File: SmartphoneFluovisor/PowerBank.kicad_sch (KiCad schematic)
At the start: 53 parts, among them J1 USB_A, J2 Conn_01x02_Pin, J3 Conn_01x02, J4 Conn_01x02_Pin, J5 Conn_01x02_Pin, J6 Conn_01x02, J7 Conn_01x02, J8 Conn_01x02_Pin, J9 Conn_01x02_Pin, SW1 SW_Push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

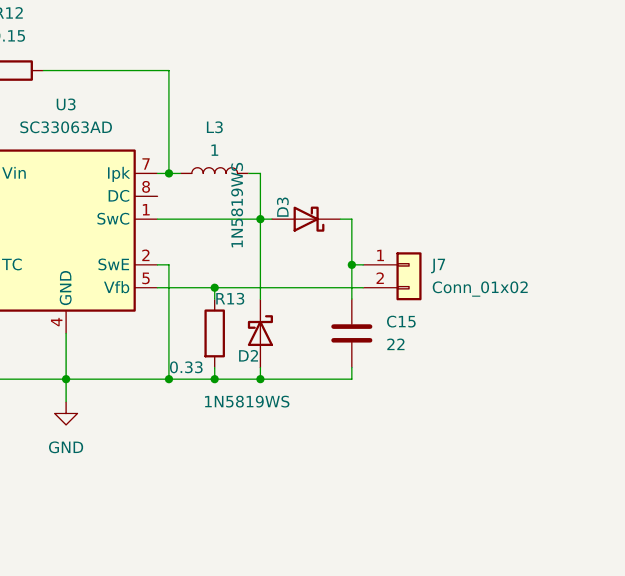
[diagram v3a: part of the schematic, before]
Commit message: v0.7 boost & buck driver are added into the PCB. Seems 2B ready!
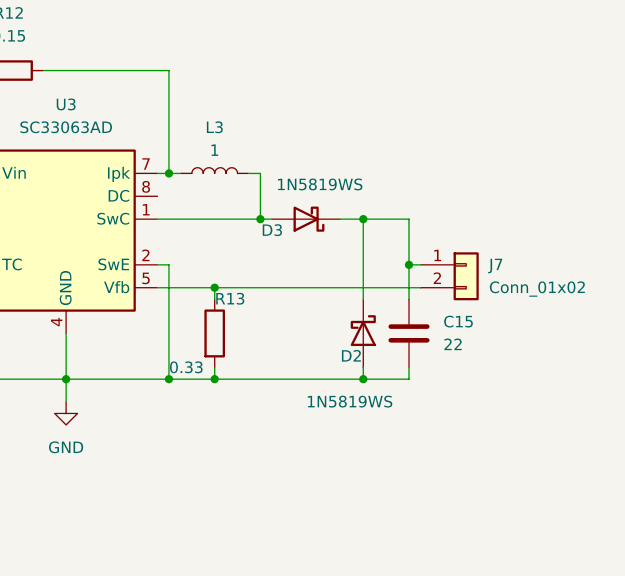
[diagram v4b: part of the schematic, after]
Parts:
- R12: footprint Resistor_SMD:R_0603_1608Metric_Pad0.98x0.95mm_HandSolder -> Resistor_SMD:R_1206_3216Metric_Pad1.30x1.75mm_HandSolder
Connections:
- net at D3.2 (A), L3.2, U3.1 (SwC): no longer D2.1 (K)
- net at C15.1, D3.1 (K), J7.1 (Pin_1): now also D2.1 (K)
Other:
- moved on the sheet: C15, D2, J7
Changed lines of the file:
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@@
   (junction (at 135.89 92.71) (diameter 0) (color 0 0 0 0)
   )
-  (junction (at 256.54 44.45) (diameter 0) (color 0 0 0 0)
+  (junction (at 262.89 44.45) (diameter 0) (color 0 0 0 0)
   )
   (junction (at 143.51 107.95) (diameter 0) (color 0 0 0 0)
@@
   (junction (at 157.48 88.9) (diameter 0) (color 0 0 0 0)
   )
+  (junction (at 257.81 39.37) (diameter 0) (color 0 0 0 0)
+  )
   (junction (at 262.89 142.24) (diameter 0) (color 0 0 0 0)
   )
@@
   (junction (at 158.75 123.19) (diameter 0) (color 0 0 0 0)
   )
-  (junction (at 246.38 57.15) (diameter 0) (color 0 0 0 0)
-  )
   (junction (at 146.05 91.44) (diameter 0) (color 0 0 0 0)
   )
@@
   (junction (at 162.56 80.01) (diameter 0) (color 0 0 0 0)
   )
+  (junction (at 257.81 57.15) (diameter 0) (color 0 0 0 0)
+  )
   (junction (at 182.88 100.33) (diameter 0) (color 0 0 0 0)
   )
@@
     (stroke (width 0) (type default))
   )
-  (wire (pts (xy 256.54 44.45) (xy 256.54 48.26))
+  (wire (pts (xy 262.89 44.45) (xy 262.89 48.26))
     (stroke (width 0) (type default))
   )
@@
     (stroke (width 0) (type default))
   )
-  (wire (pts (xy 256.54 44.45) (xy 257.81 44.45))
+  (wire (pts (xy 262.89 44.45) (xy 264.16 44.45))
     (stroke (width 0) (type default))
   )
@@
     (stroke (width 0) (type default))
   )
-  (wire (pts (xy 256.54 55.88) (xy 256.54 57.15))
+  (wire (pts (xy 262.89 55.88) (xy 262.89 57.15))
     (stroke (width 0) (type default))
   )
@@
     (stroke (width 0) (type default))
   )
-  (wire (pts (xy 246.38 39.37) (xy 246.38 48.26))
-    (stroke (width 0) (type default))
-  )
   (wire (pts (xy 222.25 144.78) (xy 218.44 144.78))
     (stroke (width 0) (type default))
@@
     (stroke (width 0) (type default))
   )
-  (wire (pts (xy 246.38 55.88) (xy 246.38 57.15))
+  (wire (pts (xy 257.81 55.88) (xy 257.81 57.15))
     (stroke (width 0) (type default))
   )
@@
     (stroke (width 0) (type default))
   )
-  (wire (pts (xy 246.38 57.15) (xy 256.54 57.15))
-    (stroke (width 0) (type default))
-  )
   (wire (pts (xy 219.71 120.65) (xy 219.71 132.08))
     (stroke (width 0) (type default))
@@
     (stroke (width 0) (type default))
   )
-  (wire (pts (xy 255.27 39.37) (xy 256.54 39.37))
+  (wire (pts (xy 255.27 39.37) (xy 257.81 39.37))
     (stroke (width 0) (type default))
   )
@@
     (stroke (width 0) (type default))
   )
+  (wire (pts (xy 257.81 39.37) (xy 262.89 39.37))
+    (stroke (width 0) (type default))
+  )
   (wire (pts (xy 143.51 107.95) (xy 152.4 107.95))
     (stroke (width 0) (type default))
@@
     (stroke (width 0) (type default))
   )
+  (wire (pts (xy 257.81 39.37) (xy 257.81 48.26))
+    (stroke (width 0) (type default))
+  )
   (wire (pts (xy 83.82 99.06) (xy 93.98 99.06))
     (stroke (width 0) (type default))
@@
     (stroke (width 0) (type default))
   )
+  (wire (pts (xy 257.81 57.15) (xy 262.89 57.15))
+    (stroke (width 0) (type default))
+  )
   (wire (pts (xy 101.6 85.09) (xy 101.6 87.63))
     (stroke (width 0) (type default))
@@
     (stroke (width 0) (type default))
   )
-  (wire (pts (xy 241.3 57.15) (xy 246.38 57.15))
+  (wire (pts (xy 241.3 57.15) (xy 257.81 57.15))
     (stroke (width 0) (type default))
   )
@@
     (stroke (width 0) (type default))
   )
-  (wire (pts (xy 256.54 39.37) (xy 256.54 44.45))
+  (wire (pts (xy 262.89 39.37) (xy 262.89 44.45))
     (stroke (width 0) (type default))
   )
@@
     (stroke (width 0) (type default))
   )
+  (wire (pts (xy 241.3 46.99) (xy 264.16 46.99))
+    (stroke (width 0) (type default))
+  )
   (wire (pts (xy 207.01 31.75) (xy 207.01 34.29))
     (stroke (width 0) (type default))
@@
     (stroke (width 0) (type default))
   )
-  (wire (pts (xy 241.3 46.99) (xy 257.81 46.99))
-    (stroke (width 0) (type default))
-  )
   (wire (pts (xy 182.88 88.9) (xy 182.88 90.17))
     (stroke (width 0) (type default))
@@
       (effects (font (size 1.27 1.27)))
     )
-    (property "Footprint" "Resistor_SMD:R_0603_1608Metric_Pad0.98x0.95mm_HandSolder" (at 218.44 21.082 90)
+    (property "Footprint" "Resistor_SMD:R_1206_3216Metric_Pad1.30x1.75mm_HandSolder" (at 218.44 21.082 90)
       (effects (font (size 1.27 1.27)) hide)
     )
@@
     )
   )
-  (symbol (lib_id "Diode:1N5819WS") (at 246.38 52.07 270) (unit 1)
+  (symbol (lib_id "Diode:1N5819WS") (at 257.81 52.07 270) (unit 1)
     (in_bom yes) (on_board yes) (dnp no)
-    (property "Reference" "D2" (at 243.84 54.61 90)
-      (effects (font (size 1.27 1.27)) (justify left))
-    )
-    (property "Value" "1N5819WS" (at 240.03 59.69 90)
-      (effects (font (size 1.27 1.27)) (justify left))
-    )
-    (property "Footprint" "Diode_SMD:D_SOD-323_HandSoldering" (at 241.935 52.07 0)
-      (effects (font (size 1.27 1.27)) hide)
-    )
-    (property "Datasheet" "https://datasheet.lcsc.com/lcsc/2204281430_Guangdong-Hottech-1N5819WS_C191023.pdf" (at 246.38 52.07 0)
+    (property "Reference" "D2" (at 255.27 54.61 90)
+      (effects (font (size 1.27 1.27)) (justify left))
+    )
+    (property "Value" "1N5819WS" (at 251.46 59.69 90)
+      (effects (font (size 1.27 1.27)) (justify left))
+    )
+    (property "Footprint" "Diode_SMD:D_SOD-323_HandSoldering" (at 253.365 52.07 0)
+      (effects (font (size 1.27 1.27)) hide)
+    )
+    (property "Datasheet" "https://datasheet.lcsc.com/lcsc/2204281430_Guangdong-Hottech-1N5819WS_C191023.pdf" (at 257.81 52.07 0)
       (effects (font (size 1.27 1.27)) hide)
     )
@@
     )
   )
-  (symbol (lib_id "Connector_Generic:Conn_01x02") (at 262.89 44.45 0) (unit 1)
-    (in_bom yes) (on_board yes) (dnp no) (fields_autoplaced)
-    (property "Reference" "J7" (at 265.43 44.45 0)
-      (effects (font (size 1.27 1.27)) (justify left))
-    )
-    (property "Value" "Conn_01x02" (at 265.43 46.99 0)
-      (effects (font (size 1.27 1.27)) (justify left))
-    )
-    (property "Footprint" "Connector_PinHeader_2.54mm:PinHeader_1x02_P2.54mm_Vertical" (at 262.89 44.45 0)
-      (effects (font (size 1.27 1.27)) hide)
-    )
-    (property "Datasheet" "~" (at 262.89 44.45 0)
+  (symbol (lib_id "Connector_Generic:Conn_01x02") (at 269.24 44.45 0) (unit 1)
+    (in_bom yes) (on_board yes) (dnp no) (fields_autoplaced)
+    (property "Reference" "J7" (at 271.78 44.45 0)
+      (effects (font (size 1.27 1.27)) (justify left))
+    )
+    (property "Value" "Conn_01x02" (at 271.78 46.99 0)
+      (effects (font (size 1.27 1.27)) (justify left))
+    )
+    (property "Footprint" "Connector_PinHeader_2.54mm:PinHeader_1x02_P2.54mm_Vertical" (at 269.24 44.45 0)
+      (effects (font (size 1.27 1.27)) hide)
+    )
+    (property "Datasheet" "~" (at 269.24 44.45 0)
       (effects (font (size 1.27 1.27)) hide)
     )
@@
   (symbol (lib_id "Diode:1N5819WS") (at 251.46 39.37 180) (unit 1)
     (in_bom yes) (on_board yes) (dnp no)
-    (property "Reference" "D3" (at 248.92 36.83 90)
-      (effects (font (size 1.27 1.27)) (justify left))
-    )
-    (property "Value" "1N5819WS" (at 243.84 33.02 90)
+    (property "Reference" "D3" (at 248.92 40.64 0)
+      (effects (font (size 1.27 1.27)) (justify left))
+    )
+    (property "Value" "1N5819WS" (at 257.81 35.56 0)
       (effects (font (size 1.27 1.27)) (justify left))
     )
@@
     )
   )
-  (symbol (lib_id "Device:C") (at 256.54 52.07 0) (unit 1)
-    (in_bom yes) (on_board yes) (dnp no) (fields_autoplaced)
-    (property "Reference" "C15" (at 260.35 50.8 0)
-      (effects (font (size 1.27 1.27)) (justify left))
-    )
-    (property "Value" "22" (at 260.35 53.34 0)
-      (effects (font (size 1.27 1.27)) (justify left))
-    )
-    (property "Footprint" "Capacitor_SMD:C_1206_3216Metric_Pad1.33x1.80mm_HandSolder" (at 257.5052 55.88 0)
-      (effects (font (size 1.27 1.27)) hide)
-    )
-    (property "Datasheet" "~" (at 256.54 52.07 0)
-      (effects (font (size 1.27 1.27)) hide)
-    )
+  (symbol (lib_id "Device:C") (at 262.89 52.07 0) (unit 1)
+    (in_bom yes) (on_board yes) (dnp no) (fields_autoplaced)
+    (property "Reference" "C15" (at 266.7 50.8 0)
+      (effects (font (size 1.27 1.27)) (justify left))
+    )
+    (property "Value" "22" (at 266.7 53.34 0)
+      (effects (font (size 1.27 1.27)) (justify left))
+    )
+    (property "Footprint" "Capacitor_SMD:C_1206_3216Metric_Pad1.33x1.80mm_HandSolder" (at 263.8552 55.88 0)
+      (effects (font (size 1.27 1.27)) hide)
+    )
+    (property "Datasheet" "~" (at 262.89 52.07 0)
+      (effects (font (size 1.27 1.27)) hide)
+    )
